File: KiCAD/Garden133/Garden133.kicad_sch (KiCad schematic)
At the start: 15 parts, among them U1 SHTC3, U2 RFM95W-915S2

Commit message: Board version 5
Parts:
- added Ca3, Ca5: 100nF, Capacitor_SMD:C_0603_1608Metric_Pad1.08x0.95mm_HandSolder, symbol Device:C
- added R2u2: 20k, Resistor_SMD:R_0603_1608Metric, symbol Device:R
- added R2v1: 200k, Resistor_SMD:R_0603_1608Metric, symbol Device:R
- added Ru1, Ru2, Ru3, Ru4, Ru6: 10k, Resistor_SMD:R_0603_1608Metric, symbol Device:R
- added Rv1: 100k, Resistor_SMD:R_0603_1608Metric, symbol Device:R
- R2v2: renamed from RM2; value 20k -> 200k
- R2v3: renamed from Ru3; value 10k -> 200k
- S_debug1: value BlueToggle -> SW_DPDT; footprint chl33_library:BlueToggle -> AliExpressSwitch:SW_SPDT_5.8x5.8_locking; symbol chl33:BlueToggle -> Switch:SW_Push_DPDT
- S_solar1: value BlueToggle -> SW_DPDY; footprint chl33_library:BlueToggle -> AliExpressSwitch:SW_SPDT_5.8x5.8_locking; symbol chl33:BlueToggle -> Switch:SW_Push_DPDT
- renumbered Ca5 to Ca1, Ca3 to Ca2, C_A1 to Ca4, Ru2 to Ru5
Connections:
- net +3.3V: now also Ru1.2, Ru2.2, Ru3.2, Ru4.2
- net +5V: now also R2v3.2
- net AMOIST: now also Ru6.2; no longer R2v3.2
- net GND: now also Ca3.1, Ca5.1, R2u2.1, R2v1.1; no longer S_solar1.4 (NCB), S_solar1.5 (INB)
- net GPIO18: now also Ru1.1
- net GPIO19: now also Ru3.1
- net GPIO23: now also Ru2.1
- net GPIO5: now also Ru4.1
- net VBATTERY+: now also Rv1.2; no longer S_solar1.2 (INA)
- net VSOLAR+: now also S_solar1.2 (B)
- net GPIO33 renamed GPIO26
- new net ADC1_CH5: Ca3.2, R2v1.2, Rv1.1
- new net ADC1_CH6: Ca5.2, R2u2.2, Ru6.1
- no-connect marks 11 -> 13
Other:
- note added: "Pull-up resistors to keep radio pins from floating."
- note removed: "VBAT-"

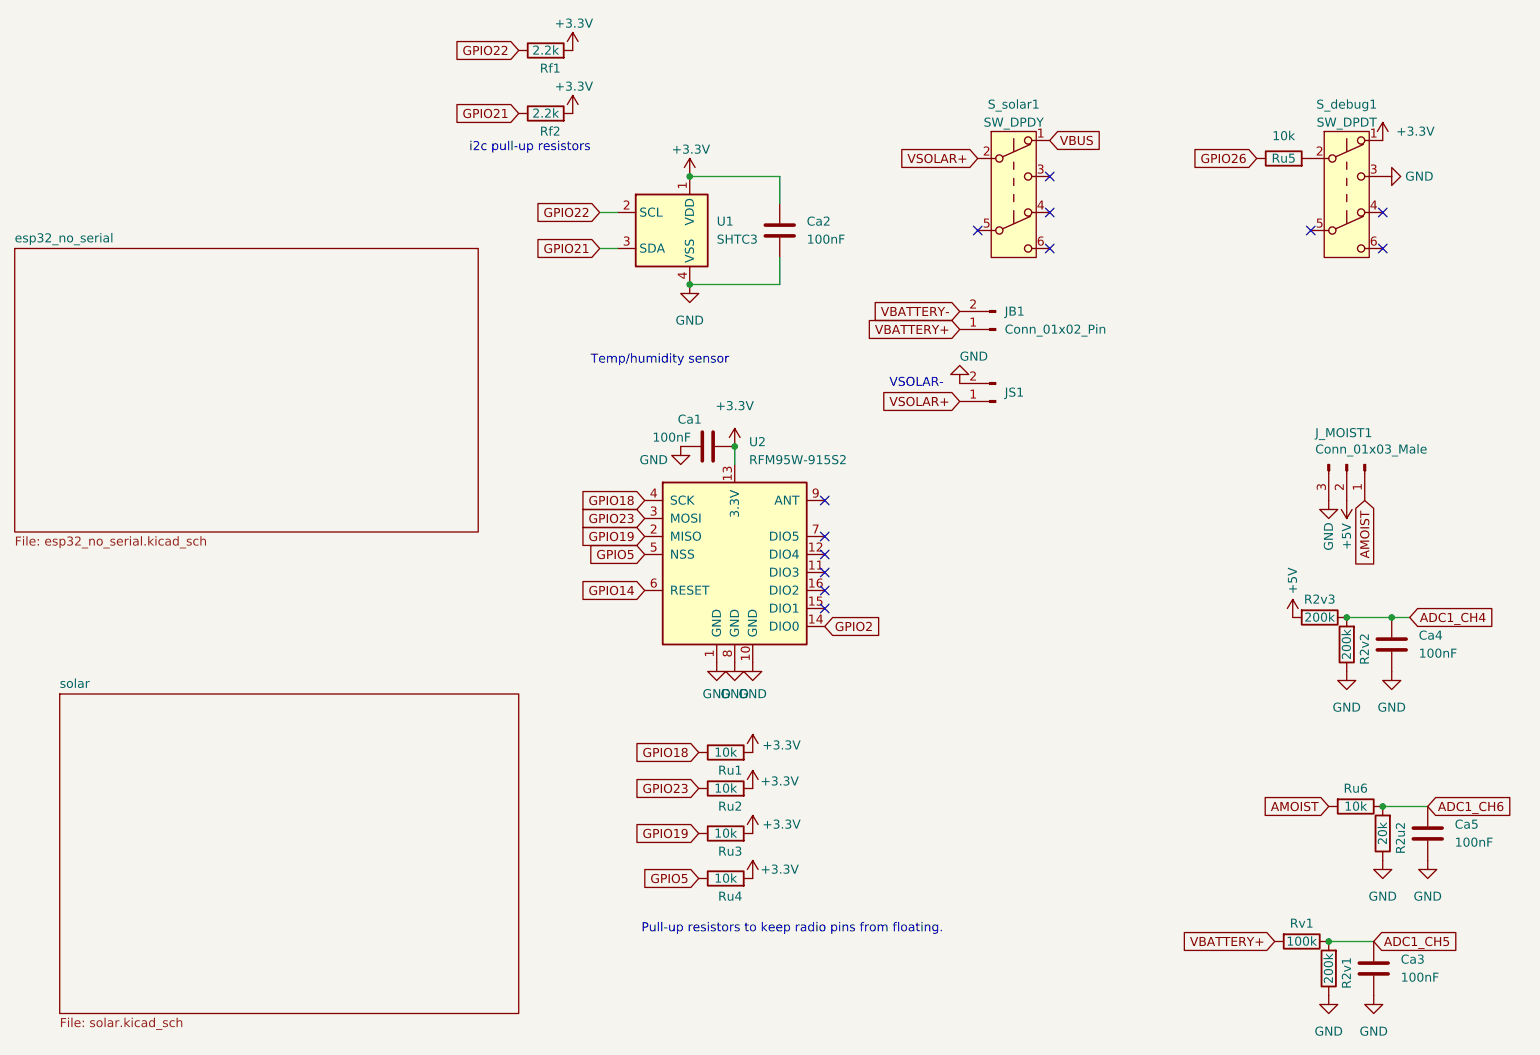
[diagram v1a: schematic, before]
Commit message: Update for board v6
- Added OpenSCAD models for Solar panel mount, tray for board+battery
- ADC Adjustment because using 220k resistors, not 200k.
- Licenses updated
- Remove support for v4 boards, update ADC slopes
- Board v6.0 (ordered)
- Support publishing more data via LoRa.
  Not able to include solar, due to packet size limitations.
- og3 version -> 0.3.10
- add raw_counts to packet
- add a filter for the moisture readings
- support normal mode -- deep sleep
  Normal mode is enabled based on the reading of the debug switch
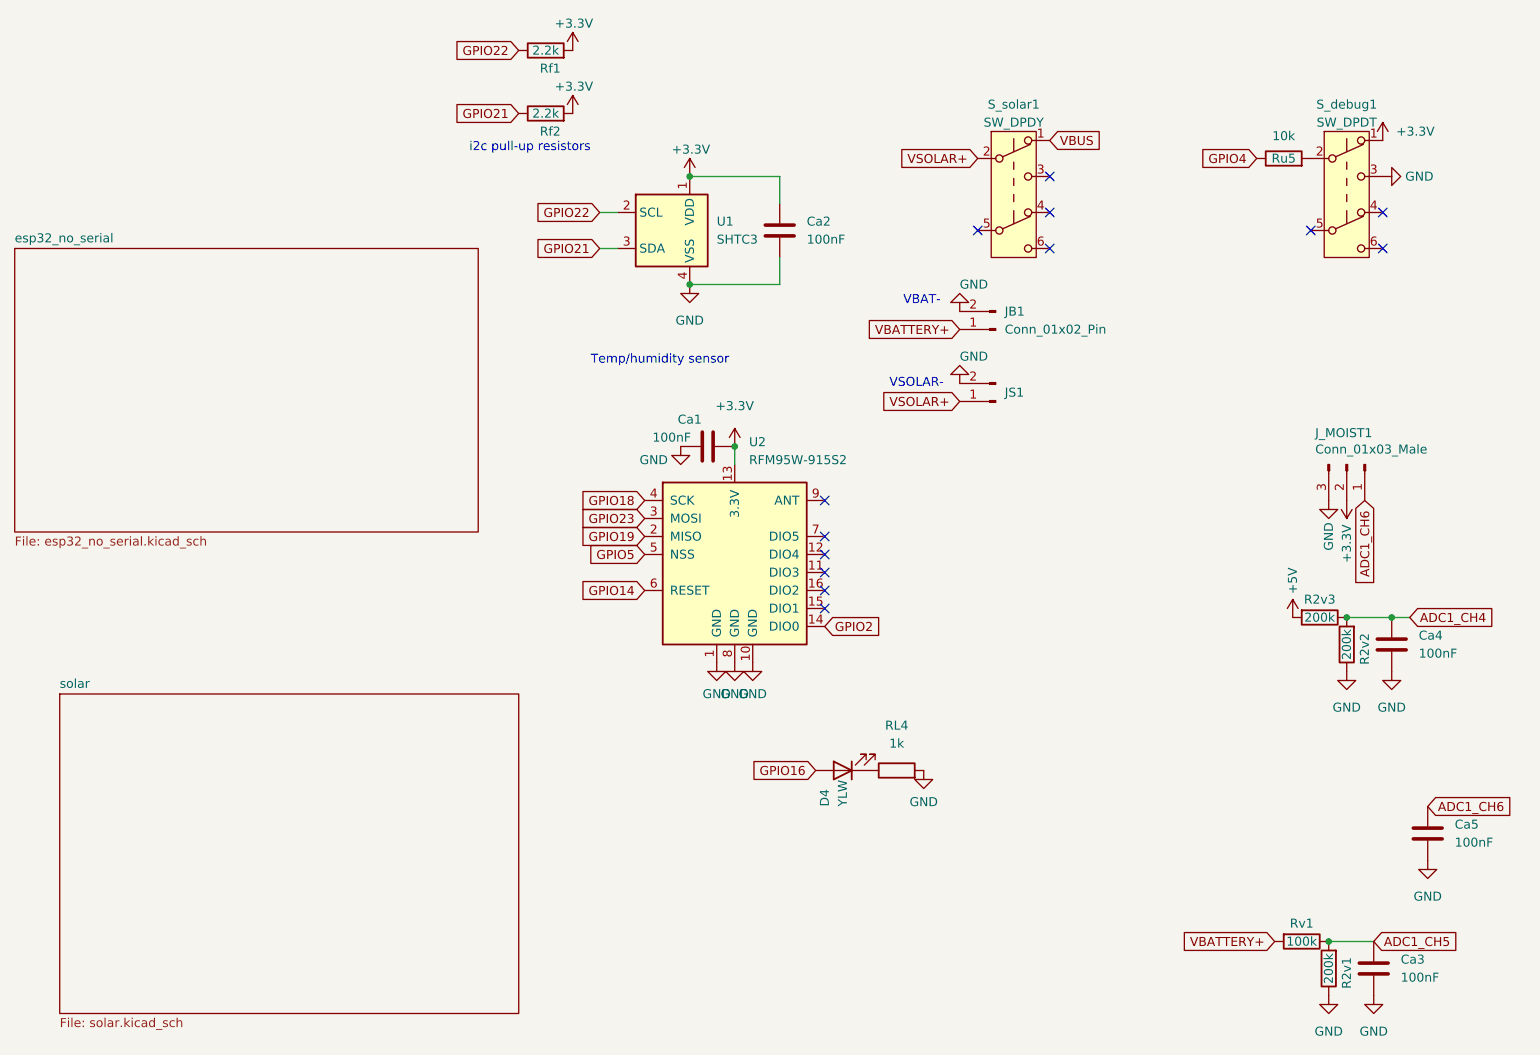
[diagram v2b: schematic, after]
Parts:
- removed R2u2: 20k, Resistor_SMD:R_0603_1608Metric, symbol Device:R
- removed Ru1, Ru2, Ru3, Ru4, Ru6: 10k, Resistor_SMD:R_0603_1608Metric, symbol Device:R
- added D4: YLW, LED_SMD:LED_0603_1608Metric_Pad1.05x0.95mm_HandSolder, symbol Device:LED
- added RL4: 1k, Resistor_SMD:R_0603_1608Metric_Pad0.98x0.95mm_HandSolder, symbol Device:R
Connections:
- net AMOIST is gone; now on net ADC1_CH6: J_MOIST1.1 (Pin_1)
- net VBATTERY- is gone; now on net GND: JB1.2 (Pin_2)
- net +3.3V: now also J_MOIST1.2 (Pin_2)
- net +5V: no longer J_MOIST1.2 (Pin_2)
- net GND: now also RL4.2
- net GPIO26 renamed GPIO4
- new net: D4.1 (K), RL4.1
- new net GPIO16: D4.2 (A)
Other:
- note added: "VBAT-"
- note removed: "Pull-up resistors to keep radio pins from floating."

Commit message: Update PCB
- Button controls power to 3.3V LDO
- DIO readings for STDBY and CHRG
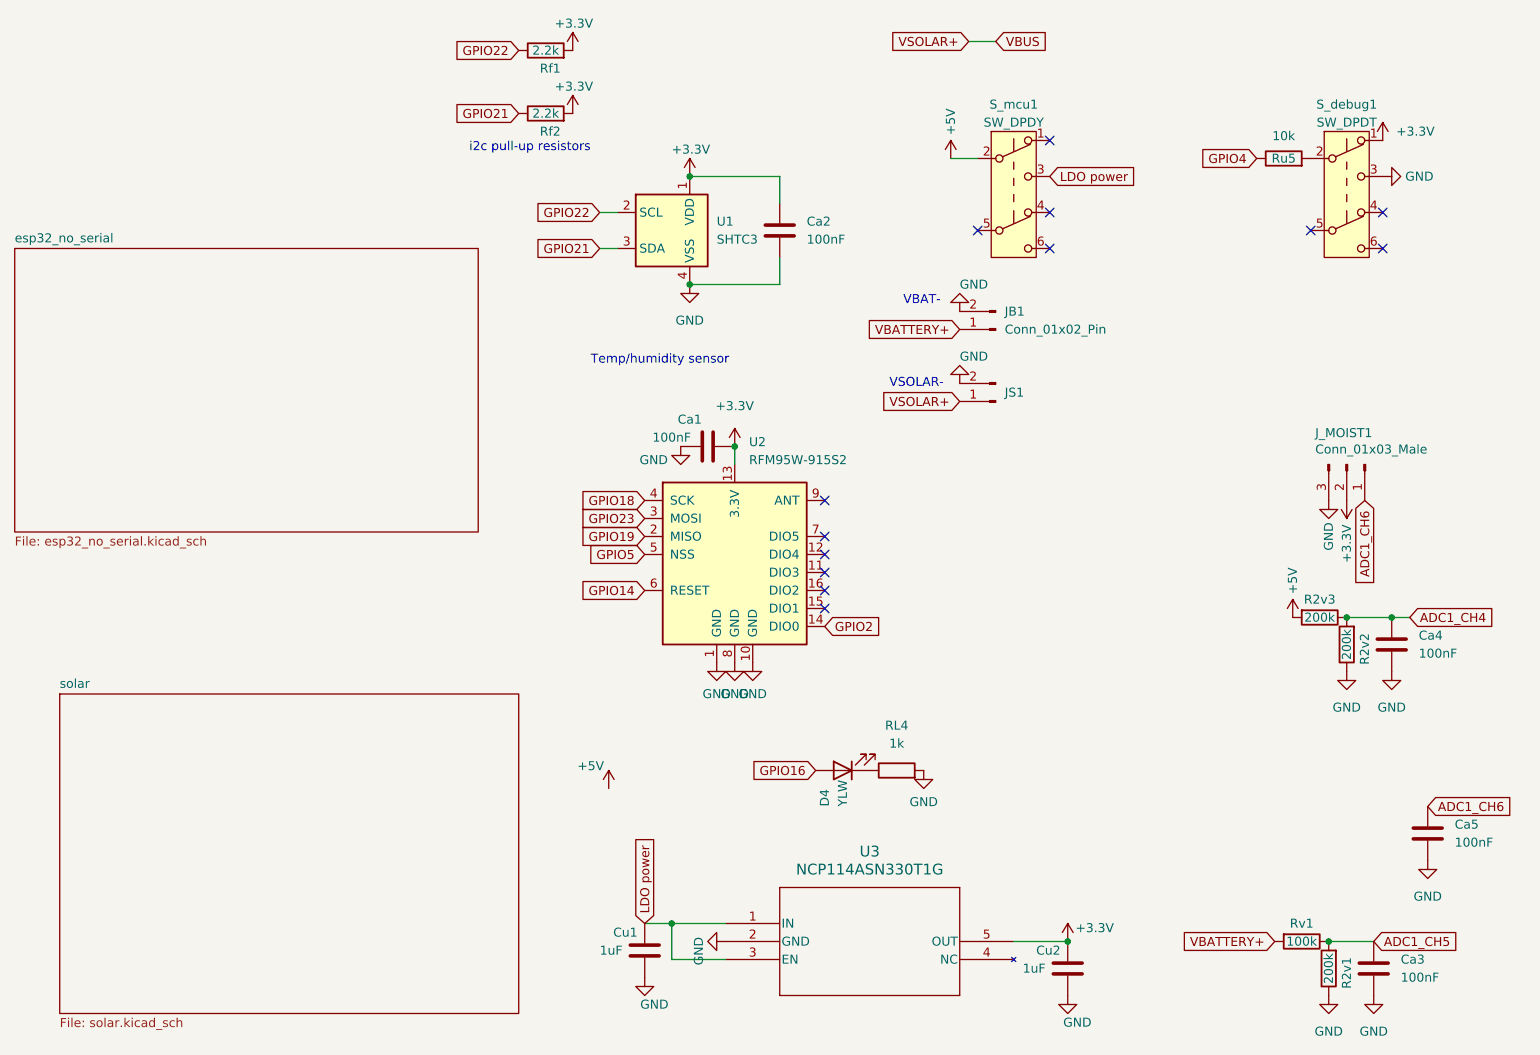
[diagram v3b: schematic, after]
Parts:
- added Cu1, Cu2: 1uF, Capacitor_SMD:C_0805_2012Metric_Pad1.18x1.45mm_HandSolder, symbol Device:C
- added U3: NCP114ASN330T1G, Package_TO_SOT_SMD:TSOT-23-5, symbol chl33:NCP114ASN330T1G
- renumbered S_solar1 to S_mcu1
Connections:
- net +3.3V: now also Cu2.1, U3.5 (OUT)
- net +5V: now also S_mcu1.2 (B)
- net GND: now also Cu1.2, Cu2.2, U3.2 (GND)
- net VBUS: now also JS1.1 (Pin_1); no longer S_mcu1.1 (A)
- net LDO power: now reaches S_mcu1.3 (C)
- net LDO power: now also Cu1.1, U3.1 (IN), U3.3 (EN)
- removed net VSOLAR+: JS1.1 (Pin_1), S_mcu1.2 (B)

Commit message: Garden133 Board v6.2 (ordered from PCBWay)
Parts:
- added Ru1, Ru2, Ru3: 10k, Resistor_SMD:R_0603_1608Metric, symbol Device:R
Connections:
- net +3.3V: now also Ru1.1, Ru2.1, Ru3.1
- net GPIO18: now also Ru3.2
- net GPIO19: now also Ru2.2
- net GPIO23: now also Ru1.2
